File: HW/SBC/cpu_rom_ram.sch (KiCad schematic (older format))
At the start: 6 parts, among them U1 WD65C02_, U2 28C256, U3 HM62256BLP-7

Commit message: New board layout with decoupling caps in the right place. Updates to the RTC code (IRQ still doesn't work).
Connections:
- net labels added: RAM
- wire segments 94 -> 95
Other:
- moved on the sheet: C11
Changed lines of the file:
@@
-	1    0    0    -1
-$EndComp
-$Comp
-L HM62256BLP-7 U3
-U 1 1 58D5907B
-P 8475 2200
-F 0 "U3" H 8175 3100 50  0000 C CNN
-F 1 "HM62256BLP-7" H 8600 1400 50  0000 C CNN
-F 2 "Housings_DIP:DIP-28_W15.24mm" H 8475 2200 50  0001 C CIN
-F 3 "" H 8475 2200 50  0001 C CNN
-	1    8475 2200
 	1    0    0    -1
 $EndComp
@@
 $EndComp
 Wire Wire Line
-	5775 3850 4050 3850
-Wire Wire Line
-	4050 3850 4050 1050
+	4050 3850 5775 3850
+Wire Wire Line
+	4050 1050 4050 3850
 Wire Wire Line
 	4050 1050 5775 1050
@@
 L C C11
 U 1 1 59052F49
-P 8475 3400
-F 0 "C11" H 8500 3500 50  0000 L CNN
-F 1 "0.1uF" H 8500 3300 50  0000 L CNN
-F 2 "Capacitors_ThroughHole:C_Disc_D3.8mm_W2.6mm_P2.50mm" H 8513 3250 50  0001 C CNN
-F 3 "" H 8475 3400 50  0001 C CNN
-	1    8475 3400
-	1    0    0    -1
-$EndComp
-Wire Wire Line
-	8475 3550 9600 3550
-Wire Wire Line
-	9600 3550 9600 1050
-Wire Wire Line
-	9600 1050 8475 1050
+P 9750 3350
+F 0 "C11" H 9775 3450 50  0000 L CNN
+F 1 "0.1uF" H 9775 3250 50  0000 L CNN
+F 2 "Capacitors_ThroughHole:C_Disc_D3.8mm_W2.6mm_P2.50mm" H 9788 3200 50  0001 C CNN
+F 3 "" H 9750 3350 50  0001 C CNN
+	1    9750 3350
+	1    0    0    -1
+$EndComp
 Wire Wire Line
 	5075 3000 4050 3000
 Connection ~ 4050 3000
 $Comp
-L GND #PWR?
+L GND #PWR01
 U 1 1 5924D5BB
 P 1525 3350
-F 0 "#PWR?" H 1525 3100 50  0001 C CNN
+F 0 "#PWR01" H 1525 3100 50  0001 C CNN
 F 1 "GND" H 1525 3225 50  0000 C CNN
 F 2 "" H 1525 3350 50  0001 C CNN
@@
 $EndComp
 $Comp
-L VCC #PWR?
+L VCC #PWR02
 U 1 1 5924D609
 P 1150 3250
-F 0 "#PWR?" H 1150 3100 50  0001 C CNN
+F 0 "#PWR02" H 1150 3100 50  0001 C CNN
 F 1 "VCC" H 1150 3400 50  0000 C CNN
 F 2 "" H 1150 3250 50  0001 C CNN
@@
 	0    -1   -1   0
 $EndComp
+$Comp
+L GND #PWR03
+U 1 1 5924DBE5
+P 5775 3550
+F 0 "#PWR03" H 5775 3300 50  0001 C CNN
+F 1 "GND" H 5775 3425 50  0000 C CNN
+F 2 "" H 5775 3550 50  0001 C CNN
+F 3 "" H 5775 3550 50  0001 C CNN
+	1    5775 3550
+	0    1    1    0
+$EndComp
+$Comp
+L VCC #PWR04
+U 1 1 5924DCC6
+P 5775 1050
+F 0 "#PWR04" H 5775 900 50  0001 C CNN
+F 1 "VCC" V 5700 1125 50  0000 C CNN
+F 2 "" H 5775 1050 50  0001 C CNN
+F 3 "" H 5775 1050 50  0001 C CNN
+	1    5775 1050
+	0    1    1    0
+$EndComp
+$Comp
+L VCC #PWR05
+U 1 1 5924DE07
+P 8475 1050
+F 0 "#PWR05" H 8475 900 50  0001 C CNN
+F 1 "VCC" H 8475 1200 50  0000 C CNN
+F 2 "" H 8475 1050 50  0001 C CNN
+F 3 "" H 8475 1050 50  0001 C CNN
+	1    8475 1050
+	1    0    0    -1
+$EndComp
+Wire Wire Line
+	8475 3250 8475 3500
+Wire Wire Line
+	8475 3500 9750 3500
+Text Label 9375 3500 0    60   ~ 0
+RAM
+Wire Wire Line
+	9750 1050 9750 3200
+Wire Wire Line
+	8475 1050 9750 1050
+Text Label 9400 1050 0    60   ~ 0
+RAM
+$Comp
+L HM62256BLP-7 U3
+U 1 1 58D5907B
+P 8475 2200
+F 0 "U3" H 8175 3100 50  0000 C CNN
+F 1 "HM62256BLP-7" H 8600 1400 50  0000 C CNN
+F 2 "Housings_DIP:DIP-28_W15.24mm" H 8475 2200 50  0001 C CIN
+F 3 "" H 8475 2200 50  0001 C CNN
+	1    8475 2200
+	1    0    0    -1
+$EndComp
+$Comp
+L GND #PWR06
+U 1 1 5927DF13
+P 8475 3250
+F 0 "#PWR06" H 8475 3000 50  0001 C CNN
+F 1 "GND" H 8475 3125 50  0000 C CNN
+F 2 "" H 8475 3250 50  0001 C CNN
+F 3 "" H 8475 3250 50  0001 C CNN
+	1    8475 3250
+	0    1    1    0
+$EndComp
 $EndSCHEMATC

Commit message: New schema. Adding a VIA and sound chip.
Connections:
- net labels added: A[0..15], D[0..7], ~RESET
- net labels removed: PHI2, ~RES
- wire segments 95 -> 94
- no-connect marks 5 -> 6

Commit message: Moved IDE schematics (WIP) into pluto.
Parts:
- U2: symbol 28C256 -> 28C256-RESCUE-pluto
- U3: symbol HM62256BLP-7 -> HM62256BLP-7-RESCUE-pluto
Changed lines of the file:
@@
 EESchema Schematic File Version 2
+LIBS:pluto-rescue
 LIBS:power
 LIBS:device
@@
 $Descr A4 11693 8268
 encoding utf-8
-Sheet 2 7
+Sheet 2 8
 Title "CPU, ROM and RAM"
 Date "2017-03-25"
@@
 NoConn ~ 1525 2350
 $Comp
-L 28C256 U2
+L 28C256-RESCUE-pluto U2
 U 1 1 58D5901B
 P 5775 2300
+AR Path="/58D5901B" Ref="U2"  Part="1"
+AR Path="/58D5892B/58D5901B" Ref="U2"  Part="1"
 F 0 "U2" H 5500 3300 50  0000 C CNN
 F 1 "28C256" H 6075 1300 50  0000 C CNN
@@
 RAM
 $Comp
-L HM62256BLP-7 U3
+L HM62256BLP-7-RESCUE-pluto U3
 U 1 1 58D5907B
 P 8475 2200

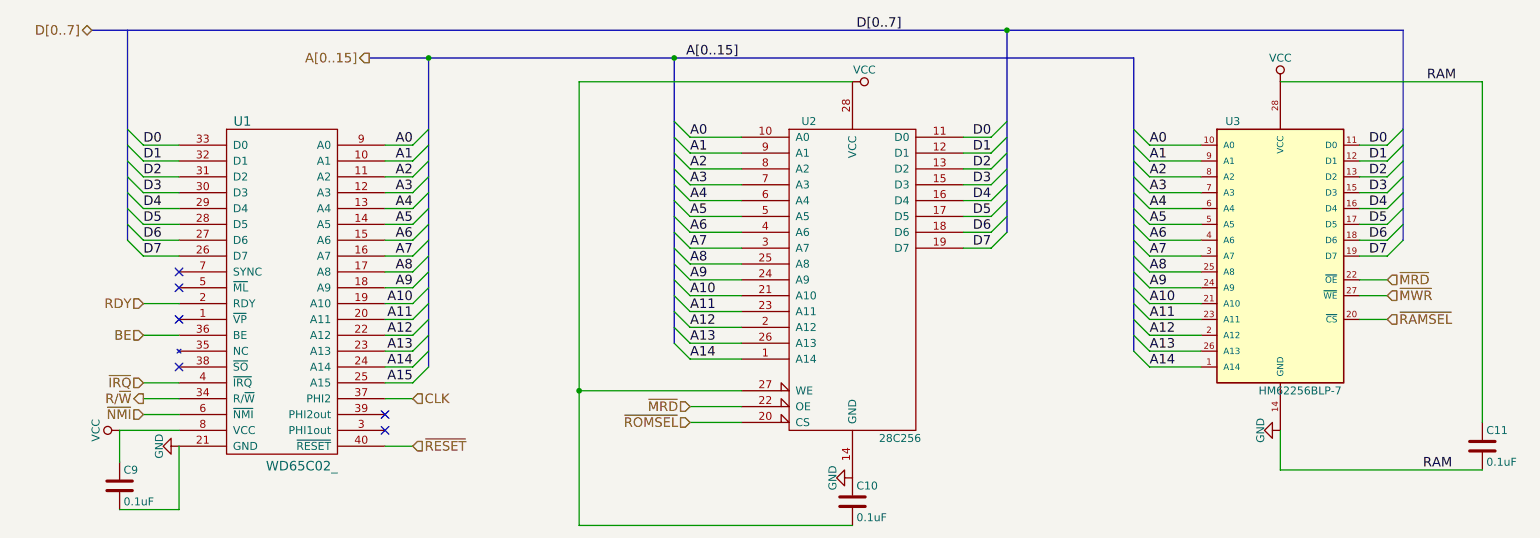
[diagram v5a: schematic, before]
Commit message: Still no VCC net in PCBnew.
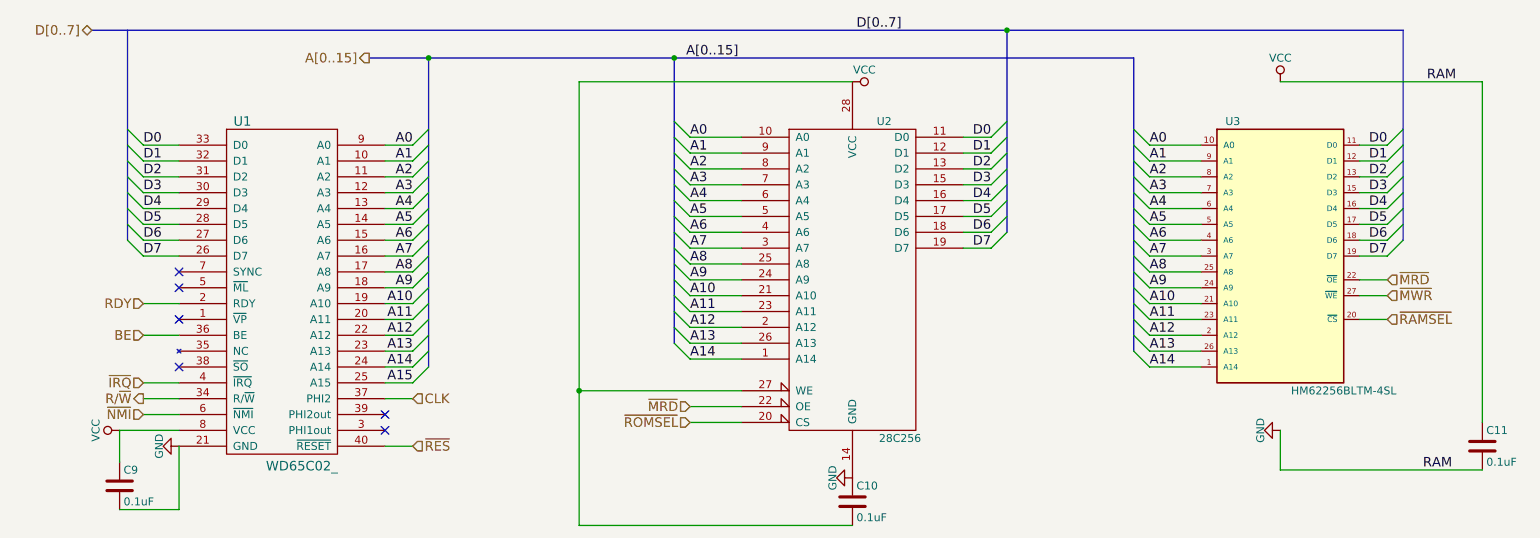
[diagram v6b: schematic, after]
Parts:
- removed U2: 28C256, Housings_DIP:DIP-28_W15.24mm, symbol 28C256-RESCUE-pluto
- removed U3: HM62256BLP-7, Housings_DIP:DIP-28_W15.24mm, symbol HM62256BLP-7-RESCUE-pluto
- added U2: 28C256, Housings_DIP:DIP-28_W15.24mm_Socket, symbol 28C256
- added U3: HM62256BLTM-4SL, Housings_DIP:DIP-28_W15.24mm_Socket, symbol HM62256BLTM-4SL
- U1: footprint Housings_DIP:DIP-40_W15.24mm -> Housings_DIP:DIP-40_W15.24mm_Socket
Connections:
- net A0: now also U2.10 (A0), U3.10 (A0)
- net A1: now also U2.9 (A1), U3.9 (A1)
- net A10: now also U2.21 (A10), U3.21 (A10)
- net A11: now also U2.23 (A11), U3.23 (A11)
- net A12: now also U2.2 (A12), U3.2 (A12)
- net A13: now also U2.26 (A13), U3.26 (A13)
- net A14: now also U2.1 (A14), U3.1 (A14)
- net A2: now also U2.8 (A2), U3.8 (A2)
- net A3: now also U2.7 (A3), U3.7 (A3)
- net A4: now also U2.6 (A4), U3.6 (A4)
- net A5: now also U2.5 (A5), U3.5 (A5)
- net A6: now also U2.4 (A6), U3.4 (A6)
- net A7: now also U2.3 (A7), U3.3 (A7)
- net A8: now also U2.25 (A8), U3.25 (A8)
- net A9: now also U2.24 (A9), U3.24 (A9)
- net D0: now also U2.11 (D0), U3.11 (D0)
- net D1: now also U2.12 (D1), U3.12 (D1)
- net D2: now also U2.13 (D2), U3.13 (D2)
- net D3: now also U2.15 (D3), U3.15 (D3)
- net D4: now also U2.16 (D4), U3.16 (D4)
- net D5: now also U2.17 (D5), U3.17 (D5)
- net D6: now also U2.18 (D6), U3.18 (D6)
- net D7: now also U2.19 (D7), U3.19 (D7)
- net GND: now also U2.14 (GND), U2.27 (WE), U2.28 (VCC), U3.14 (GND), U3.28 (VCC)
- net ~MRD: now also U2.22 (OE), U3.22 (~OE)
- net ~MWR: now also U3.27 (~WE)
- net ~RAMSEL: now also U3.20 (~CS)
- net ~ROMSEL: now also U2.20 (CS)
- net ~RESET renamed ~RES
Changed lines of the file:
@@
 EESchema Schematic File Version 2
-LIBS:pluto-rescue
 LIBS:power
 LIBS:device
@@
 LIBS:pluto
 LIBS:pluto-cache
-LIBS:IDE_interface-cache
 EELAYER 25 0
 EELAYER END
@@
 F 0 "U1" H 1925 3400 60  0000 C CNN
 F 1 "WD65C02_" H 2300 1225 60  0000 C CNN
-F 2 "Housings_DIP:DIP-40_W15.24mm" H 1625 2550 60  0001 C CNN
+F 2 "Housings_DIP:DIP-40_W15.24mm_Socket" H 1625 2550 60  0001 C CNN
 F 3 "" H 1625 2550 60  0000 C CNN
 	1    2175 2350
@@
 NoConn ~ 1525 2550
 NoConn ~ 1525 2350
-$Comp
-L 28C256-RESCUE-pluto U2
-U 1 1 58D5901B
-P 5775 2300
-AR Path="/58D5901B" Ref="U2"  Part="1"
-AR Path="/58D5892B/58D5901B" Ref="U2"  Part="1"
-F 0 "U2" H 5500 3300 50  0000 C CNN
-F 1 "28C256" H 6075 1300 50  0000 C CNN
-F 2 "Housings_DIP:DIP-28_W15.24mm" H 5775 2300 50  0001 C CNN
-F 3 "" H 5775 2300 50  0001 C CNN
-	1    5775 2300
-	1    0    0    -1
-$EndComp
 $Comp
 L C C9
@@
 Text Label 9400 1050 0    60   ~ 0
 RAM
-$Comp
-L HM62256BLP-7-RESCUE-pluto U3
-U 1 1 58D5907B
-P 8475 2200
-F 0 "U3" H 8175 3100 50  0000 C CNN
-F 1 "HM62256BLP-7" H 8600 1400 50  0000 C CNN
-F 2 "Housings_DIP:DIP-28_W15.24mm" H 8475 2200 50  0001 C CIN
-F 3 "" H 8475 2200 50  0001 C CNN
-	1    8475 2200
-	1    0    0    -1
-$EndComp
 $Comp
 L GND #PWR06
@@
 ~NMI
 Text HLabel 3000 3350 2    60   Input ~ 0
-~RESET
+~RES
 Text HLabel 3000 3050 2    60   Input ~ 0
 CLK
@@
 Text HLabel 4750 3200 0    60   Input ~ 0
 ~ROMSEL
+$Comp
+L HM62256BLTM-4SL U3
+U 1 1 59386D44
+P 8475 2200
+F 0 "U3" H 8175 3100 50  0000 C CNN
+F 1 "HM62256BLTM-4SL" H 8875 1400 50  0000 C CNN
+F 2 "Housings_DIP:DIP-28_W15.24mm_Socket" H 8475 2200 50  0001 C CIN
+F 3 "" H 8475 2200 50  0001 C CNN
+	1    8475 2200
+	1    0    0    -1
+$EndComp
+$Comp
+L 28C256 U2
+U 1 1 59386D85
+P 5775 2300
+F 0 "U2" H 5975 3300 50  0000 C CNN
+F 1 "28C256" H 6075 1300 50  0000 C CNN
+F 2 "Housings_DIP:DIP-28_W15.24mm_Socket" H 5775 2300 50  0001 C CNN
+F 3 "" H 5775 2300 50  0001 C CNN
+	1    5775 2300
+	1    0    0    -1
+$EndComp
 $EndSCHEMATC

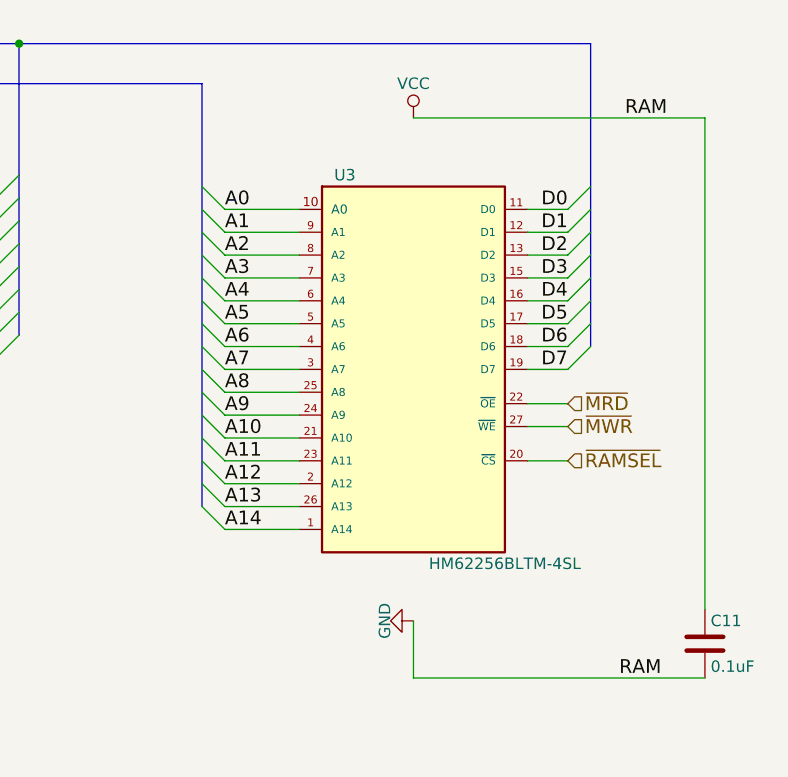
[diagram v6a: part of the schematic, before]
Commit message: New PCB layout. Added datasheet for AY-3-8912 and LM386.
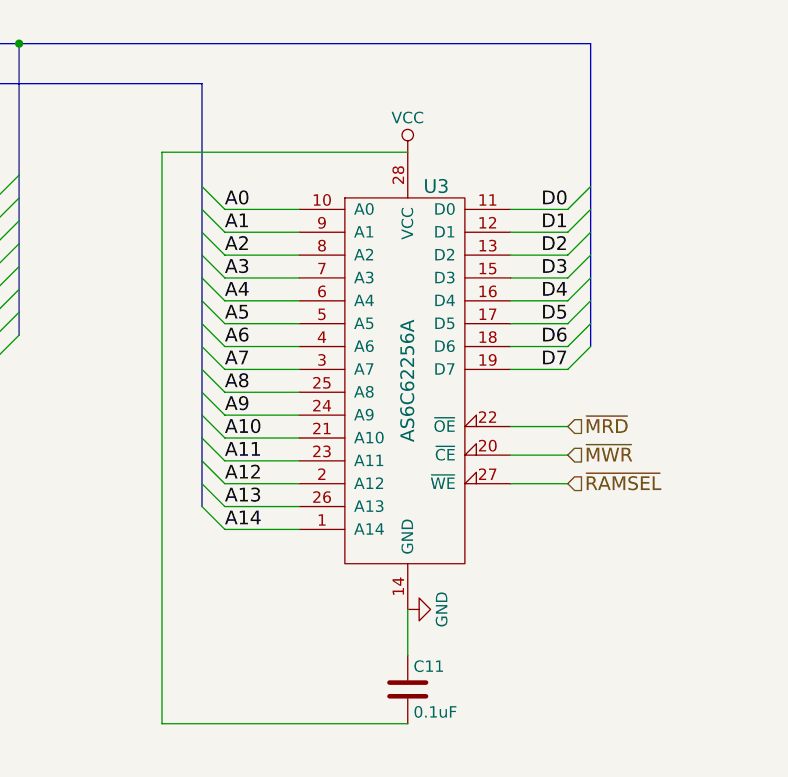
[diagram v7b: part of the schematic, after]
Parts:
- removed U3: HM62256BLTM-4SL, Housings_DIP:DIP-28_W15.24mm_Socket, symbol HM62256BLTM-4SL
- added U3: AS6C62256A, Housings_DIP:DIP-28_W15.24mm_Socket, symbol AS6C62256A
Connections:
- net A0: now also U3.10 (A0)
- net A1: now also U3.9 (A1)
- net A10: now also U3.21 (A10)
- net A11: now also U3.23 (A11)
- net A12: now also U3.2 (A12)
- net A13: now also U3.26 (A13)
- net A14: now also U3.1 (A14)
- net A2: now also U3.8 (A2)
- net A3: now also U3.7 (A3)
- net A4: now also U3.6 (A4)
- net A5: now also U3.5 (A5)
- net A6: now also U3.4 (A6)
- net A7: now also U3.3 (A7)
- net A8: now also U3.25 (A8)
- net A9: now also U3.24 (A9)
- net D0: now also U3.11 (D0)
- net D1: now also U3.12 (D1)
- net D2: now also U3.13 (D2)
- net D3: now also U3.15 (D3)
- net D4: now also U3.16 (D4)
- net D5: now also U3.17 (D5)
- net D6: now also U3.18 (D6)
- net D7: now also U3.19 (D7)
- net GND: now also U3.14 (GND); no longer C10.2, C11.2, C9.1, U1.8 (VCC), U2.27 (WE), U2.28 (VCC)
- net ~MRD: now also U3.22 (~OE)
- net ~MWR: now also U3.20 (~CE)
- net ~RAMSEL: now also U3.27 (~WE)
- new net VCC: C10.2, C11.2, C9.1, U1.8 (VCC), U2.27 (WE), U2.28 (VCC), U3.28 (VCC)
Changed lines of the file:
@@
-$EndComp
-$Comp
-L C C11
-U 1 1 59052F49
-P 9750 3350
-F 0 "C11" H 9775 3450 50  0000 L CNN
-F 1 "0.1uF" H 9775 3250 50  0000 L CNN
-F 2 "Capacitors_ThroughHole:C_Disc_D3.8mm_W2.6mm_P2.50mm" H 9788 3200 50  0001 C CNN
-F 3 "" H 9750 3350 50  0001 C CNN
-	1    9750 3350
-	1    0    0    -1
 $EndComp
 $Comp
@@
 F 3 "" H 5775 1050 50  0001 C CNN
 	1    5775 1050
-	0    1    1    0
-$EndComp
-$Comp
-L VCC #PWR05
-U 1 1 5924DE07
-P 8475 1050
-F 0 "#PWR05" H 8475 900 50  0001 C CNN
-F 1 "VCC" H 8475 1200 50  0000 C CNN
-F 2 "" H 8475 1050 50  0001 C CNN
-F 3 "" H 8475 1050 50  0001 C CNN
-	1    8475 1050
-	1    0    0    -1
-$EndComp
-Text Label 9375 3500 0    60   ~ 0
-RAM
-Text Label 9400 1050 0    60   ~ 0
-RAM
-$Comp
-L GND #PWR06
-U 1 1 5927DF13
-P 8475 3250
-F 0 "#PWR06" H 8475 3000 50  0001 C CNN
-F 1 "GND" H 8475 3125 50  0000 C CNN
-F 2 "" H 8475 3250 50  0001 C CNN
-F 3 "" H 8475 3250 50  0001 C CNN
-	1    8475 3250
 	0    1    1    0
 $EndComp
@@
 	7975 2850 7650 2850
 Wire Wire Line
-	8975 1450 9150 1450
-Wire Wire Line
-	8975 1550 9150 1550
-Wire Wire Line
-	8975 1650 9150 1650
-Wire Wire Line
-	8975 1750 9150 1750
-Wire Wire Line
-	8975 1850 9150 1850
-Wire Wire Line
-	8975 1950 9150 1950
-Wire Wire Line
-	8975 2050 9150 2050
-Wire Wire Line
-	8975 2150 9150 2150
+	8900 1450 9150 1450
+Wire Wire Line
+	8900 1550 9150 1550
+Wire Wire Line
+	8900 1650 9150 1650
+Wire Wire Line
+	8900 1750 9150 1750
+Wire Wire Line
+	8900 1850 9150 1850
+Wire Wire Line
+	8900 1950 9150 1950
+Wire Wire Line
+	8900 2050 9150 2050
+Wire Wire Line
+	8900 2150 9150 2150
 Wire Wire Line
 	6475 1400 6650 1400
@@
 	5075 3200 4750 3200
 Wire Wire Line
-	8975 2300 9150 2300
-Wire Wire Line
-	8975 2400 9150 2400
-Wire Wire Line
-	8975 2550 9150 2550
+	8900 2400 9150 2400
+Wire Wire Line
+	8900 2525 9150 2525
+Wire Wire Line
+	8900 2650 9150 2650
 Wire Wire Line
 	1150 3450 1150 3250
@@
 	5075 3000 4050 3000
 Connection ~ 4050 3000
-Wire Wire Line
-	8475 3250 8475 3500
-Wire Wire Line
-	8475 3500 9750 3500
-Wire Wire Line
-	9750 1050 9750 3200
-Wire Wire Line
-	8475 1050 9750 1050
 Wire Bus Line
 	3100 900  3100 2850
@@
 CLK
 NoConn ~ 2825 3150
-Text HLabel 9150 2300 2    60   Input ~ 0
+Text HLabel 9150 2400 2    60   Input ~ 0
 ~MRD
-Text HLabel 9150 2400 2    60   Input ~ 0
+Text HLabel 9150 2525 2    60   Input ~ 0
 ~MWR
-Text HLabel 9150 2550 2    60   Input ~ 0
+Text HLabel 9150 2650 2    60   Input ~ 0
 ~RAMSEL
 Text HLabel 4750 3100 0    60   Input ~ 0
@@
 Text HLabel 4750 3200 0    60   Input ~ 0
 ~ROMSEL
-$Comp
-L HM62256BLTM-4SL U3
-U 1 1 59386D44
-P 8475 2200
-F 0 "U3" H 8175 3100 50  0000 C CNN
-F 1 "HM62256BLTM-4SL" H 8875 1400 50  0000 C CNN
-F 2 "Housings_DIP:DIP-28_W15.24mm_Socket" H 8475 2200 50  0001 C CIN
-F 3 "" H 8475 2200 50  0001 C CNN
-	1    8475 2200
-	1    0    0    -1
-$EndComp
 $Comp
 L 28C256 U2
@@
 	1    0    0    -1
 $EndComp
+$Comp
+L AS6C62256A U3
+U 1 1 59399129
+P 8450 2225
+F 0 "U3" H 8575 3100 60  0000 C CNN
+F 1 "AS6C62256A" V 8450 2250 60  0000 C CNN
+F 2 "Housings_DIP:DIP-28_W15.24mm_Socket" H 8450 2225 60  0001 C CNN
+F 3 "" H 8450 2225 60  0001 C CNN
+	1    8450 2225
+	1    0    0    -1
+$EndComp
+$Comp
+L C C11
+U 1 1 593998AF
+P 8450 3550
+F 0 "C11" H 8475 3650 50  0000 L CNN
+F 1 "0.1uF" H 8475 3450 50  0000 L CNN
+F 2 "Capacitors_ThroughHole:C_Disc_D3.8mm_W2.6mm_P2.50mm" H 8488 3400 50  0001 C CNN
+F 3 "" H 8450 3550 50  0001 C CNN
+	1    8450 3550
+	1    0    0    -1
+$EndComp
+Wire Wire Line
+	8450 3700 7375 3700
+Wire Wire Line
+	7375 3700 7375 1200
+Wire Wire Line
+	7375 1200 8450 1200
+$Comp
+L GND #PWR05
+U 1 1 5939C93B
+P 8450 3200
+F 0 "#PWR05" H 8450 2950 50  0001 C CNN
+F 1 "GND" H 8450 3050 50  0000 C CNN
+F 2 "" H 8450 3200 50  0001 C CNN
+F 3 "" H 8450 3200 50  0001 C CNN
+	1    8450 3200
+	0    -1   -1   0
+$EndComp
+Wire Wire Line
+	8450 3400 8450 3200
+$Comp
+L VCC #PWR06
+U 1 1 5939CBCE
+P 8450 1200
+F 0 "#PWR06" H 8450 1050 50  0001 C CNN
+F 1 "VCC" H 8450 1350 50  0000 C CNN
+F 2 "" H 8450 1200 50  0001 C CNN
+F 3 "" H 8450 1200 50  0001 C CNN
+	1    8450 1200
+	1    0    0    -1
+$EndComp

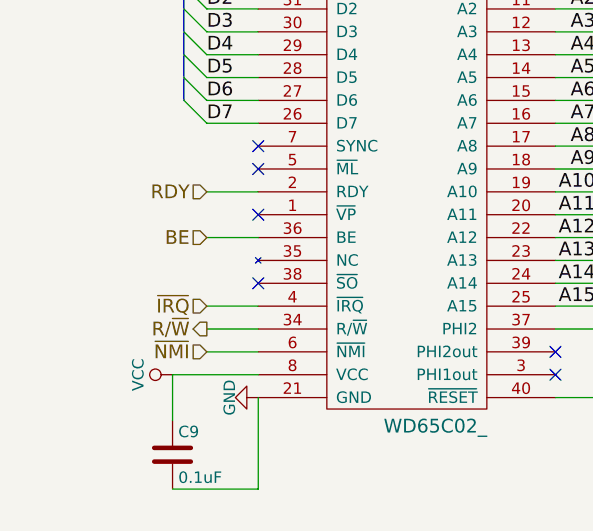
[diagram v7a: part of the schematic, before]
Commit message: Schema is now Alpha.
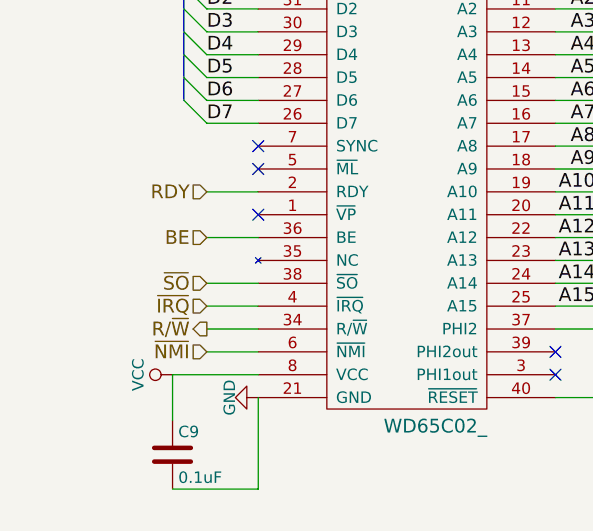
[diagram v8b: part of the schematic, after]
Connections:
- net ~SO: now reaches U1.38 (~SO)
- no-connect marks 6 -> 5
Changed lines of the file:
@@
 $EndComp
 NoConn ~ 2825 3250
-NoConn ~ 1525 2850
 NoConn ~ 1525 2250
 NoConn ~ 1525 2550
@@
 $EndComp
 $Comp
-L GND #PWR01
+L GND #PWR2
 U 1 1 5924D5BB
 P 1525 3350
-F 0 "#PWR01" H 1525 3100 50  0001 C CNN
+F 0 "#PWR2" H 1525 3100 50  0001 C CNN
 F 1 "GND" H 1525 3225 50  0000 C CNN
 F 2 "" H 1525 3350 50  0001 C CNN
@@
 $EndComp
 $Comp
-L VCC #PWR02
+L VCC #PWR1
 U 1 1 5924D609
 P 1150 3250
-F 0 "#PWR02" H 1150 3100 50  0001 C CNN
+F 0 "#PWR1" H 1150 3100 50  0001 C CNN
 F 1 "VCC" H 1150 3400 50  0000 C CNN
 F 2 "" H 1150 3250 50  0001 C CNN
@@
 $EndComp
 $Comp
-L GND #PWR03
+L GND #PWR4
 U 1 1 5924DBE5
 P 5775 3550
-F 0 "#PWR03" H 5775 3300 50  0001 C CNN
+F 0 "#PWR4" H 5775 3300 50  0001 C CNN
 F 1 "GND" H 5775 3425 50  0000 C CNN
 F 2 "" H 5775 3550 50  0001 C CNN
@@
 $EndComp
 $Comp
-L VCC #PWR04
+L VCC #PWR3
 U 1 1 5924DCC6
 P 5775 1050
-F 0 "#PWR04" H 5775 900 50  0001 C CNN
+F 0 "#PWR3" H 5775 900 50  0001 C CNN
 F 1 "VCC" V 5700 1125 50  0000 C CNN
 F 2 "" H 5775 1050 50  0001 C CNN
@@
 	7375 1200 8450 1200
 $Comp
-L GND #PWR05
+L GND #PWR6
 U 1 1 5939C93B
 P 8450 3200
-F 0 "#PWR05" H 8450 2950 50  0001 C CNN
+F 0 "#PWR6" H 8450 2950 50  0001 C CNN
 F 1 "GND" H 8450 3050 50  0000 C CNN
 F 2 "" H 8450 3200 50  0001 C CNN
@@
 	8450 3400 8450 3200
 $Comp
-L VCC #PWR06
+L VCC #PWR5
 U 1 1 5939CBCE
 P 8450 1200
-F 0 "#PWR06" H 8450 1050 50  0001 C CNN
+F 0 "#PWR5" H 8450 1050 50  0001 C CNN
 F 1 "VCC" H 8450 1350 50  0000 C CNN
 F 2 "" H 8450 1200 50  0001 C CNN
@@
 	1    0    0    -1
 $EndComp
+Text HLabel 1300 2850 0    60   Input ~ 0
+~SO
+Wire Wire Line
+	1525 2850 1300 2850
 $EndSCHEMATC
